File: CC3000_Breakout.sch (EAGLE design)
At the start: 19 parts

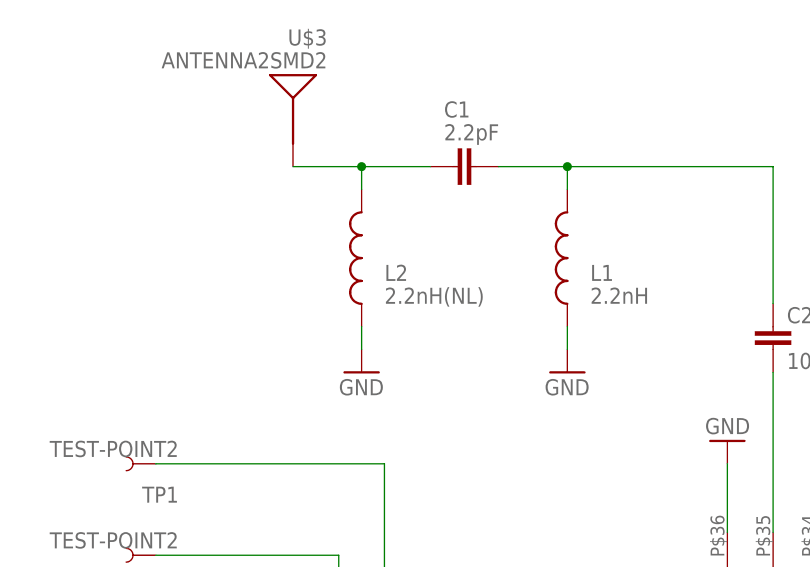
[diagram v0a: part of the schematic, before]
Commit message: Version 1.1
Removed 2nd (NL) inductor, straightened out antenna trace
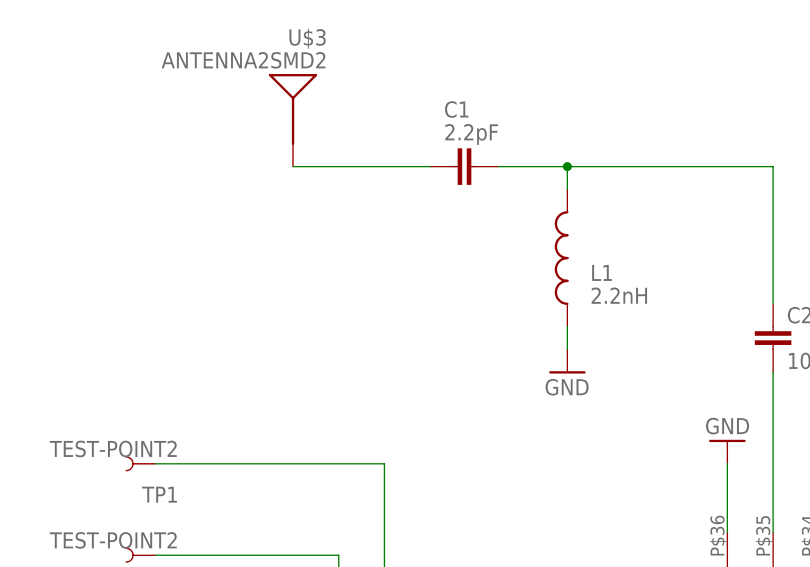
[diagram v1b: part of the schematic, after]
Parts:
- removed L2: 2.2nH(NL), SparkFun:INDUCTOR0402
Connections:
- net GND: no longer L2.1
- net N$15: no longer L2.2
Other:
- note added: "1.1"
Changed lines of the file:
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@@
 <part name="TP5" library="SparkFun-Passives" deviceset="TEST-POINT" device="2"/>
 <part name="TP3" library="SparkFun-Passives" deviceset="TEST-POINT" device="2"/>
-<part name="L2" library="SparkFun" deviceset="INDUCTOR" device="0402" value="2.2nH(NL)"/>
-<part name="GND10" library="supply1" deviceset="GND" device=""/>
 <part name="JP1" library="SparkFun-Connectors" deviceset="M04" device="PTH" value="Jumper1"/>
 <part name="JP2" library="SparkFun-Connectors" deviceset="M04" device="PTH" value="Jumper2"/>
@@
 <text x="301.26" y="23.9" size="2.54" layer="94" font="vector">cmagagna@yahoo.com</text>
 <text x="301.26" y="31.9" size="2.54" layer="94" font="vector">TI CC3000 Breakout</text>
+<text x="391.16" y="7.62" size="2.54" layer="104">1.1</text>
 </plain>
 <instances>
@@
 <instance part="TP5" gate="G$1" x="129.54" y="170.18" rot="R180"/>
 <instance part="TP3" gate="G$1" x="289.56" y="154.94"/>
-<instance part="L2" gate="G$1" x="152.4" y="223.52" smashed="yes" rot="R180">
-<attribute name="NAME" x="154.94" y="220.98" size="1.778" layer="95"/>
-<attribute name="VALUE" x="154.94" y="218.44" size="1.778" layer="96"/>
-</instance>
-<instance part="GND10" gate="1" x="152.4" y="210.82"/>
 <instance part="JP1" gate="G$1" x="73.66" y="88.9"/>
 <instance part="JP2" gate="G$1" x="363.22" y="91.44" rot="R180"/>
@@
 <pinref part="JP2" gate="G$1" pin="3"/>
 </segment>
-<segment>
-<pinref part="GND10" gate="1" pin="GND"/>
-<pinref part="L2" gate="G$1" pin="1"/>
-<wire x1="152.4" y1="213.36" x2="152.4" y2="215.9" width="0.1524" layer="91"/>
-</segment>
 </net>
 <net name="SPI_CLK" class="0">
@@
 <segment>
 <pinref part="C1" gate="G$1" pin="1"/>
-<wire x1="144.78" y1="233.68" x2="152.4" y2="233.68" width="0.1524" layer="91"/>
 <pinref part="U$3" gate="G$1" pin="SIGNAL"/>
-<pinref part="L2" gate="G$1" pin="2"/>
-<wire x1="152.4" y1="233.68" x2="160.02" y2="233.68" width="0.1524" layer="91"/>
-<wire x1="152.4" y1="231.14" x2="152.4" y2="233.68" width="0.1524" layer="91"/>
-<junction x="152.4" y="233.68"/>
-</segment>
-</net>
+<wire x1="144.78" y1="233.68" x2="160.02" y2="233.68" width="0.1524" layer="91"/>
+</segment>
+</net>

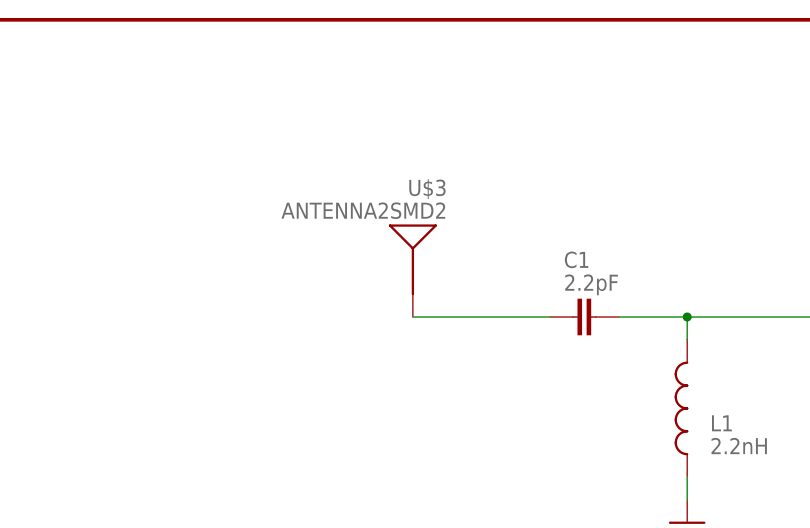
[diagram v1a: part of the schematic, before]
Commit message: Version 1.3
The antenna in Matt's design wasn't the right size, I've fixed the
antenna footprint to match the actual chip used.
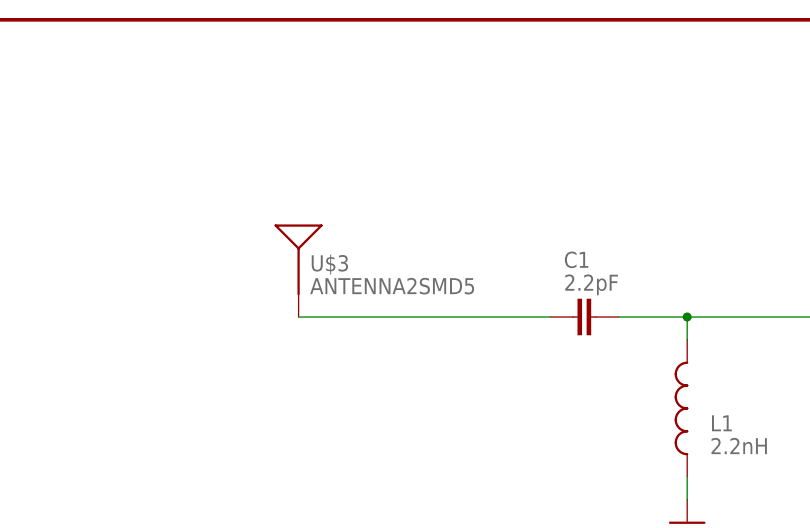
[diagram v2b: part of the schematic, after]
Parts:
- U$3: value ANTENNA2SMD2 -> ANTENNA2SMD5; device SparkFun:ANTENNA2SMD2 -> SparkFun-RF-Modified:ANTENNA2SMD5
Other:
- moved on the sheet: U$3
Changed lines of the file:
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@@
 <part name="L1" library="SparkFun" deviceset="INDUCTOR" device="0402" value="2.2nH"/>
 <part name="GND20" library="supply1" deviceset="GND" device=""/>
-<part name="U$3" library="SparkFun" deviceset="ANTENNA2" device="SMD2"/>
 <part name="P+1" library="SparkFun" deviceset="3.3V" device="" value="VCC"/>
 <part name="FUNC" library="SparkFun-Passives" deviceset="SOLDERJUMPER" device="TRACE"/>
@@
 <part name="JP1" library="SparkFun-Connectors" deviceset="M04" device="PTH" value="Jumper1"/>
 <part name="JP2" library="SparkFun-Connectors" deviceset="M04" device="PTH" value="Jumper2"/>
+<part name="U$3" library="SparkFun-RF-Modified" deviceset="ANTENNA2" device="SMD5"/>
 </parts>
 <sheets>
@@
 </instance>
 <instance part="GND20" gate="1" x="175.26" y="210.82"/>
-<instance part="U$3" gate="G$1" x="144.78" y="238.76" smashed="yes">
-<attribute name="NAME" x="148.59" y="248.92" size="1.778" layer="95" rot="R180"/>
-<attribute name="VALUE" x="148.59" y="246.38" size="1.778" layer="96" rot="R180"/>
-</instance>
 <instance part="P+1" gate="G$1" x="322.58" y="152.4"/>
 <instance part="FUNC" gate="1" x="106.68" y="142.24"/>
@@
 <instance part="JP1" gate="G$1" x="73.66" y="88.9"/>
 <instance part="JP2" gate="G$1" x="363.22" y="91.44" rot="R180"/>
+<instance part="U$3" gate="G$1" x="132.08" y="238.76"/>
 </instances>
 <busses>
@@
 <segment>
 <pinref part="C1" gate="G$1" pin="1"/>
+<wire x1="132.08" y1="233.68" x2="160.02" y2="233.68" width="0.1524" layer="91"/>
 <pinref part="U$3" gate="G$1" pin="SIGNAL"/>
-<wire x1="144.78" y1="233.68" x2="160.02" y2="233.68" width="0.1524" layer="91"/>
-</segment>
-</net>
+</segment>
+</net>

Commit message: Abandoned project!
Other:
- note added: "1.4"
- note removed: "1.1"
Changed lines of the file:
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@@
 <?xml version="1.0" encoding="utf-8"?>
 <!DOCTYPE eagle SYSTEM "eagle.dtd">
-<eagle version="6.3">
+<eagle version="6.4">
 <drawing>
 <settings>
@@
 <clearance class="1" value="0.2032"/>
 </class>
-<class number="2" name="antenna" width="0.36321875" drill="0">
-<clearance class="2" value="0.3048"/>
+<class number="2" name="antenna" width="0.95" drill="0">
+<clearance class="2" value="0.1524"/>
 </class>
 <class number="3" name="1.8v" width="0.4572" drill="0">
@@
 <text x="301.26" y="23.9" size="2.54" layer="94" font="vector">cmagagna@yahoo.com</text>
 <text x="301.26" y="31.9" size="2.54" layer="94" font="vector">TI CC3000 Breakout</text>
-<text x="391.16" y="7.62" size="2.54" layer="104">1.1</text>
+<text x="391.16" y="7.62" size="2.54" layer="104">1.4</text>
 </plain>
 <instances>
